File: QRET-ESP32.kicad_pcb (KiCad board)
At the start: 4 copper layers, 131 parts, among them J1 Conn_01x04, J10 Conn_01x04, J2 Conn_01x02, J3 Conn_02x01, J4 Conn_01x02, J5 Conn_01x02, J6 Conn_01x02, J7 Conn_02x04_Counter_Clockwise, J8 Conn_02x04_Counter_Clockwise, J9 Conn_01x04, Q1 BSS138, Q2 DMP6023LE-13, Q3 BSS138, Q4 BSS138, Q5 BSS138, U1 ESP32-S2-DevKitC-1, U2 LM3880-1AA, U3 LMR33630BDDA, U4 LMR33630BDDA, U5 TPS78533QKVURQ1, U6 TPS78450QDBVRQ1, U7 ADS112C04, U8 ADS112C04, U9 ADS112C04

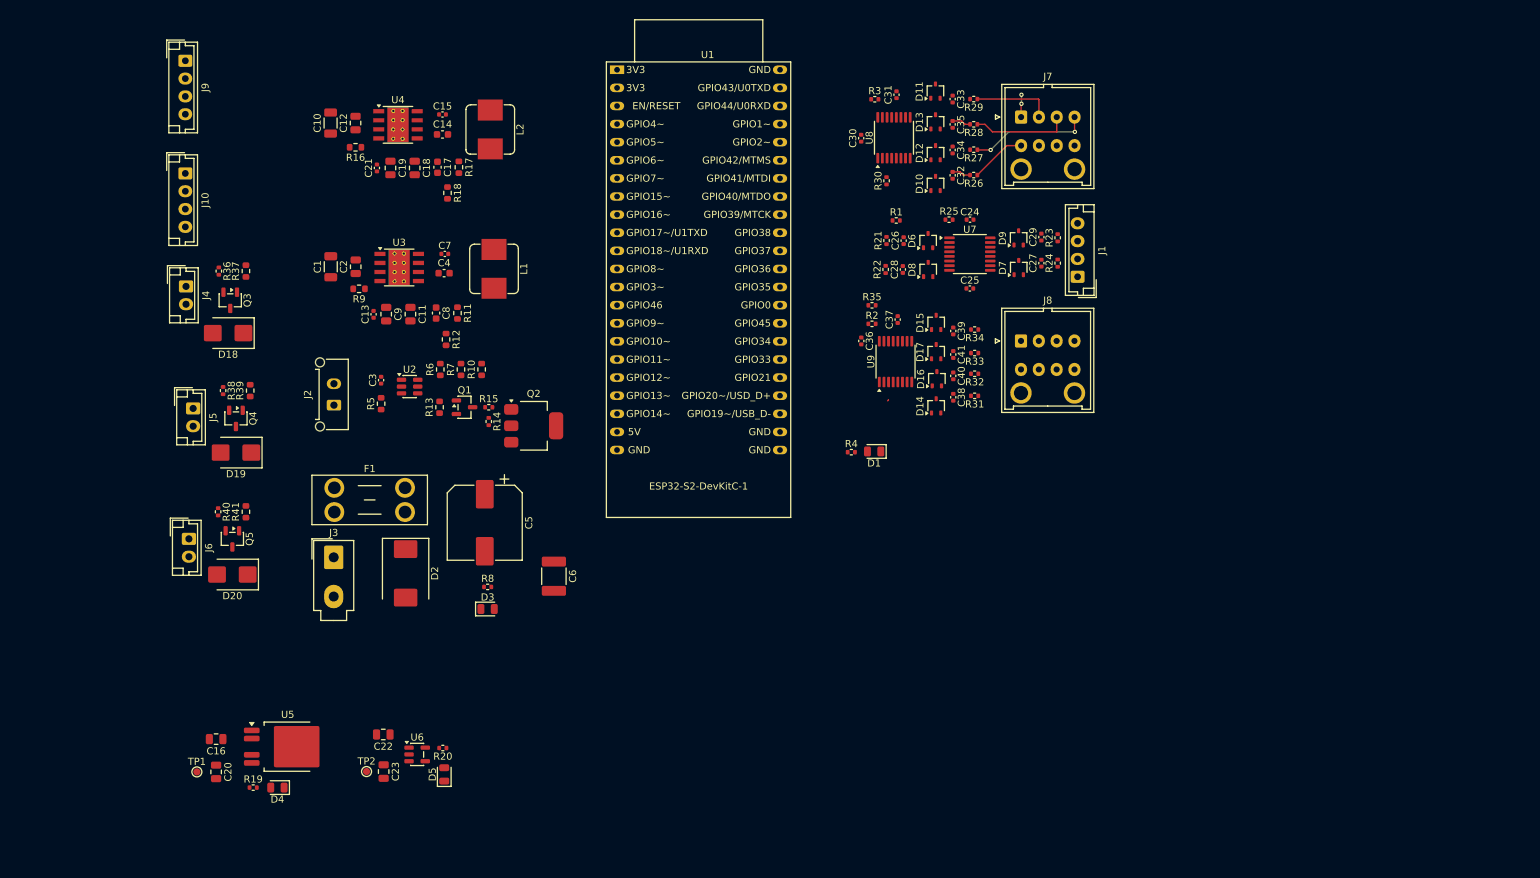
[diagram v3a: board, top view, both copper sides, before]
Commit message: Initial PCB placement and wiring.
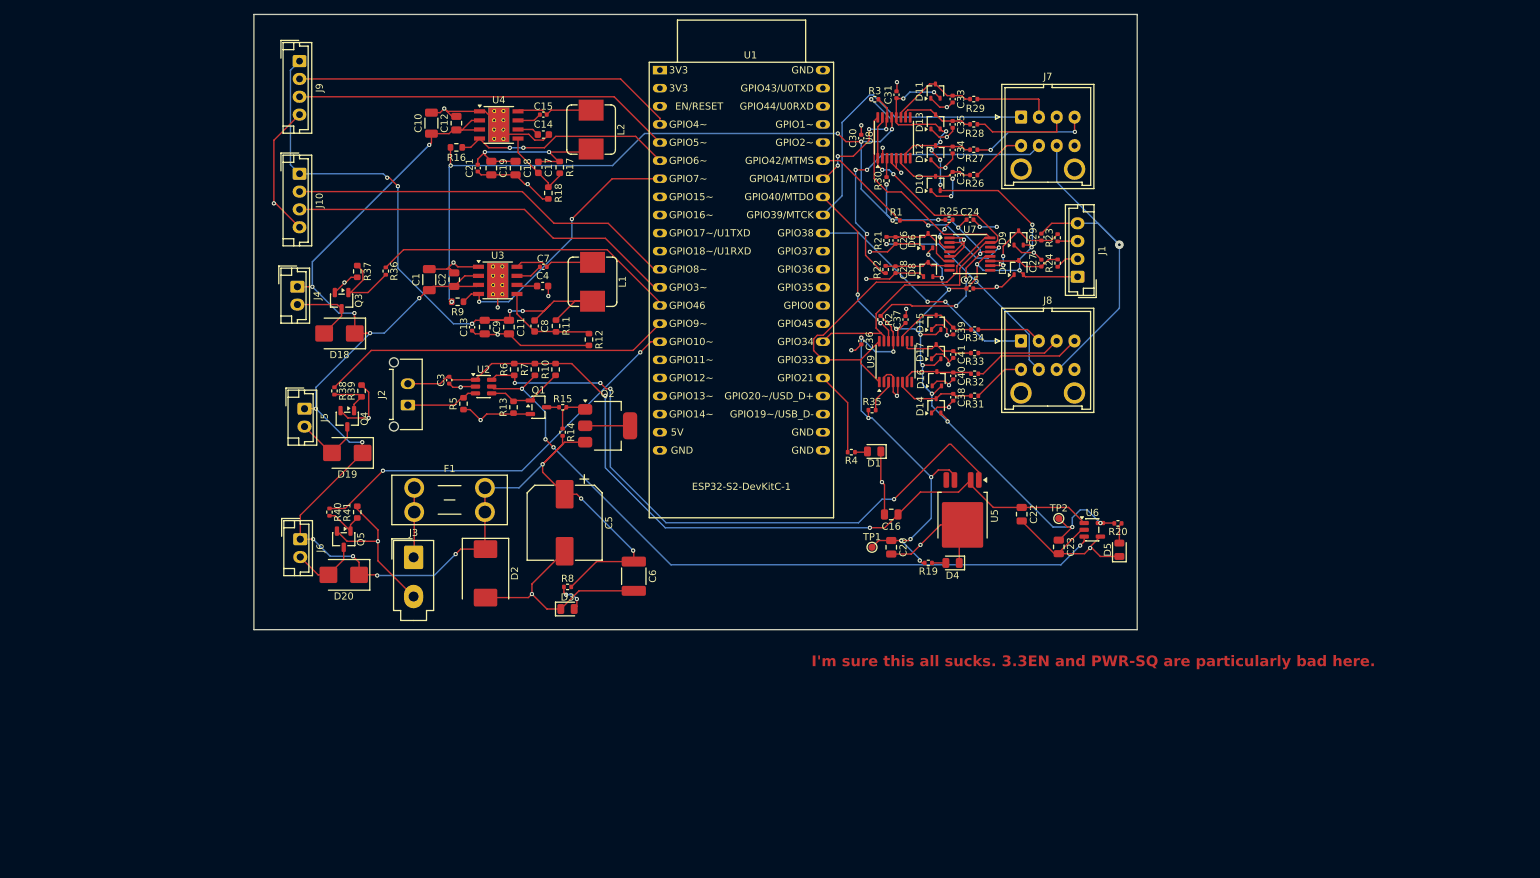
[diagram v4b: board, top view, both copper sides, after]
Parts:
- moved TP2 103.4 mm to (212.5, 106.3)
- moved U5 100.0 mm to (199.0, 105.9), turned to -90 degrees
- moved D4 99.8 mm to (197.6, 112.5)
- moved R19 99.8 mm to (194.2, 112.5), turned to 180 degrees
- moved R20 99.8 mm to (220.8, 107.0)
- moved TP1 99.8 mm to (186.3, 110.3)
- moved U6 99.8 mm to (217.2, 107.9)
- moved C16 99.8 mm to (189.0, 105.7)
- moved C20 99.8 mm to (189.0, 110.3)
- moved C23 99.8 mm to (212.5, 110.3)
- moved D5 99.8 mm to (221.0, 110.7)
- moved C22 94.7 mm to (207.3, 105.7), turned to -90 degrees
- moved R36 23.4 mm to (118.1, 71.6)
- moved R12 20.0 mm to (146.6, 81.2)
- moved J10 16.0 mm to (106.0, 58.0)
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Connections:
- C11 pad 1: /Power_Regulation/+12.0V -> +12V
- C13 pad 2: /Power_Regulation/+12.0V -> +12V
- C8 pad 1: /Power_Regulation/+12.0V -> +12V
- C9 pad 1: /Power_Regulation/+12.0V -> +12V
- J1 pad 1: /Load_Cell/5V_In -> +5V
- L1 pad 2: /Power_Regulation/+12.0V -> +12V
- R11 pad 1: /Power_Regulation/+12.0V -> +12V
- U1 pad 12: unconnected-(U1-GPIO8/ADC1_CH7-Pad12) -> Fan_2_Control
- U1 pad 13: unconnected-(U1-GPIO3/ADC1_CH2-Pad13) -> Fan_2_PWM
- U1 pad 14: unconnected-(U1-GPIO46-Pad14) -> A1_Control
- U1 pad 15: 24V_GOOD -> A2_Control
- U1 pad 16: 12V_GOOD -> Nitrous_Control
- U1 pad 30: Nitrous_Control -> unconnected-(U1-GPIO45-Pad30)
- U1 pad 31: A2_Control -> unconnected-(U1-GPIO0-Pad31)
- U1 pad 32: A1_Control -> unconnected-(U1-GPIO35-Pad32)
- U1 pad 33: Fan_2_PWM -> unconnected-(U1-GPIO36-Pad33)
- U1 pad 34: Fan_1_PWM -> unconnected-(U1-GPIO37-Pad34)
- U1 pad 4: unconnected-(U1-GPIO4/ADC1_CH3-Pad4) -> Fan_1_Control
- U1 pad 40: Fan_2_Control -> unconnected-(U1-GPIO2/ADC1_CH1-Pad40)
- U1 pad 41: Fan_1_Control -> unconnected-(U1-GPIO1/ADC1_CH0-Pad41)
- U1 pad 5: unconnected-(U1-GPIO5/ADC1_CH4-Pad5) -> Fan_1_PWM
- U1 pad 6: unconnected-(U1-GPIO6/ADC1_CH5-Pad6) -> 24V_GOOD
- U1 pad 7: unconnected-(U1-GPIO7/ADC1_CH6-Pad7) -> 12V_GOOD
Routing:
- net GND: track 0.19 -> 362.4 mm, vias 0 -> 40
- net +3.3V: track 0.00 -> 212.4 mm, vias 0 -> 20
- net +24V: track 0.00 -> 207.5 mm, vias 0 -> 14
- net +5V: track 0.00 -> 159.0 mm, vias 0 -> 21
- net /Power_Regulation/PWR_SQ: track 0.00 -> 117.5 mm, vias 0 -> 2
- net /Power_Regulation/+5V_EN: track 0.00 -> 100.4 mm, vias 0 -> 4
- net /Power_Regulation/+3.3V_EN: track 0.00 -> 91.4 mm, vias 0 -> 4
- net +12V: track 0.00 -> 88.0 mm, vias 0 -> 5
- net I2C_Clock: track 0.00 -> 76.3 mm
- net I2C_Data: track 0.00 -> 64.2 mm, vias 0 -> 2
- net Nitrous_Control: track 0.00 -> 56.0 mm, vias 0 -> 2
- net Fan_2_PWM: track 0.00 -> 55.1 mm
- net Fan_2_Control: track 0.00 -> 55.1 mm
- net Fan_1_Control: track 0.00 -> 53.7 mm
- net Fan_1_PWM: track 0.00 -> 53.2 mm
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- added copper zone on In1.Cu, net GND
- added copper zone on In2.Cu, net GND
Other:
- board outline added: 123.9 x 86.3 mm
- board text added: "I'm sure this all sucks. 3.3EN and PWR-SQ are particularly bad here."

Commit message: Updated power regulation, To-Do: Rewire PCB
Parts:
- removed Q1: BSS138, Package_TO_SOT_SMD:SOT-23-3
- removed Q2: DMP6023LE-13, Package_TO_SOT_SMD:SOT-223-3_TabPin2
- removed R13: 470k, Resistor_SMD:R_0603_1608Metric
- removed R14, R15: 10k, Resistor_SMD:R_0402_1005Metric
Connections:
- C16 pad 1: /Power_Regulation/PWR_SQ -> /Power_Regulation/+5.3V
- C22 pad 1: /Power_Regulation/PWR_SQ -> /Power_Regulation/+5.3V
- C3 pad 2: /Power_Regulation/PWR_SQ -> /Power_Regulation/+5.3V
- J2 pad 2: /Power_Regulation/PWR_SQ -> /Power_Regulation/+5.3V
- R10 pad 1: Net-(Q1-G) -> /Power_Regulation/+12_EN
- R10 pad 2: /Power_Regulation/PWR_SQ -> /Power_Regulation/+5.3V
- R6 pad 2: /Power_Regulation/PWR_SQ -> /Power_Regulation/+5.3V
- R7 pad 2: /Power_Regulation/PWR_SQ -> /Power_Regulation/+5.3V
- U2 pad 1: /Power_Regulation/PWR_SQ -> /Power_Regulation/+5.3V
- U2 pad 4: Net-(Q1-G) -> /Power_Regulation/+12_EN
- U3 pad 3: +24V -> /Power_Regulation/+12_EN
- U5 pad 2: /Power_Regulation/PWR_SQ -> /Power_Regulation/+5.3V
- U6 pad 1: /Power_Regulation/PWR_SQ -> /Power_Regulation/+5.3V
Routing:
- net /Power_Regulation/PWR_SQ: track 117.5 -> 0.00 mm, vias 2 -> 0
- net /Power_Regulation/+5.3V: track 27.4 -> 144.9 mm, vias 2 -> 4
- net +24V: track 207.5 -> 191.5 mm
- net Net-(Q1-G): track 10.9 -> 0.00 mm
- net /Power_Regulation/+12_EN: track 0.00 -> 10.9 mm
- net GND: track 362.4 -> 354.5 mm
- net +24V_PT: track 6.30 -> 0.00 mm
- net Net-(Q2-G): track 5.97 -> 0.00 mm
- net Net-(Q1-D): track 1.75 -> 0.00 mm
- net +5V: vias 21 -> 20
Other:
- board text added: "Ground Support Equipment ESP32 Board Version 1"
